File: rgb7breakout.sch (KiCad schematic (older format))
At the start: 2 parts

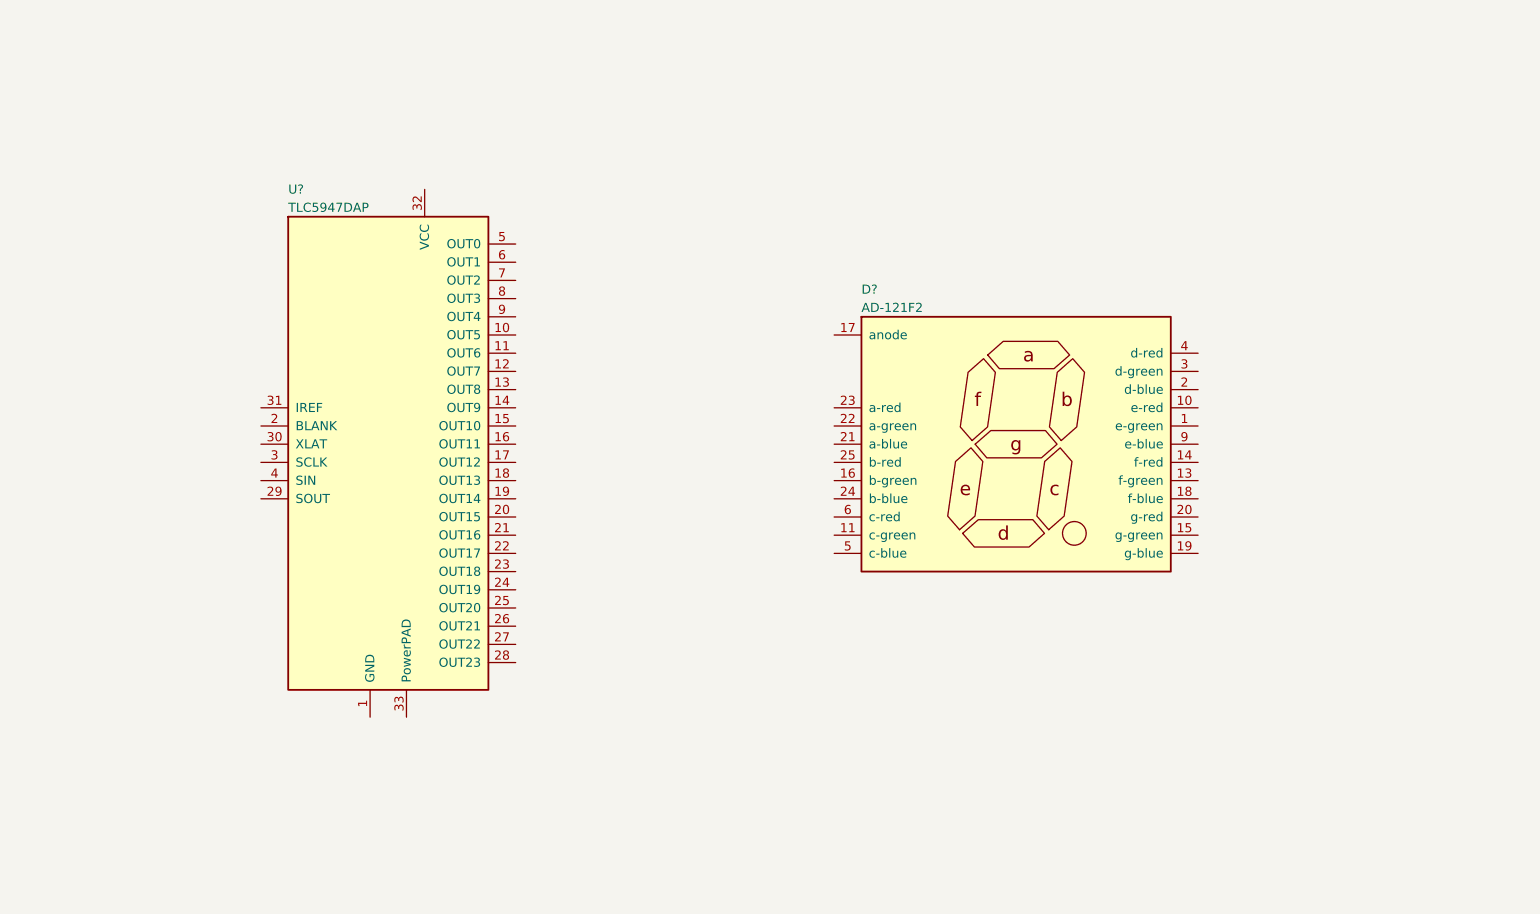
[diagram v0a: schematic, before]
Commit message: add RGB LED
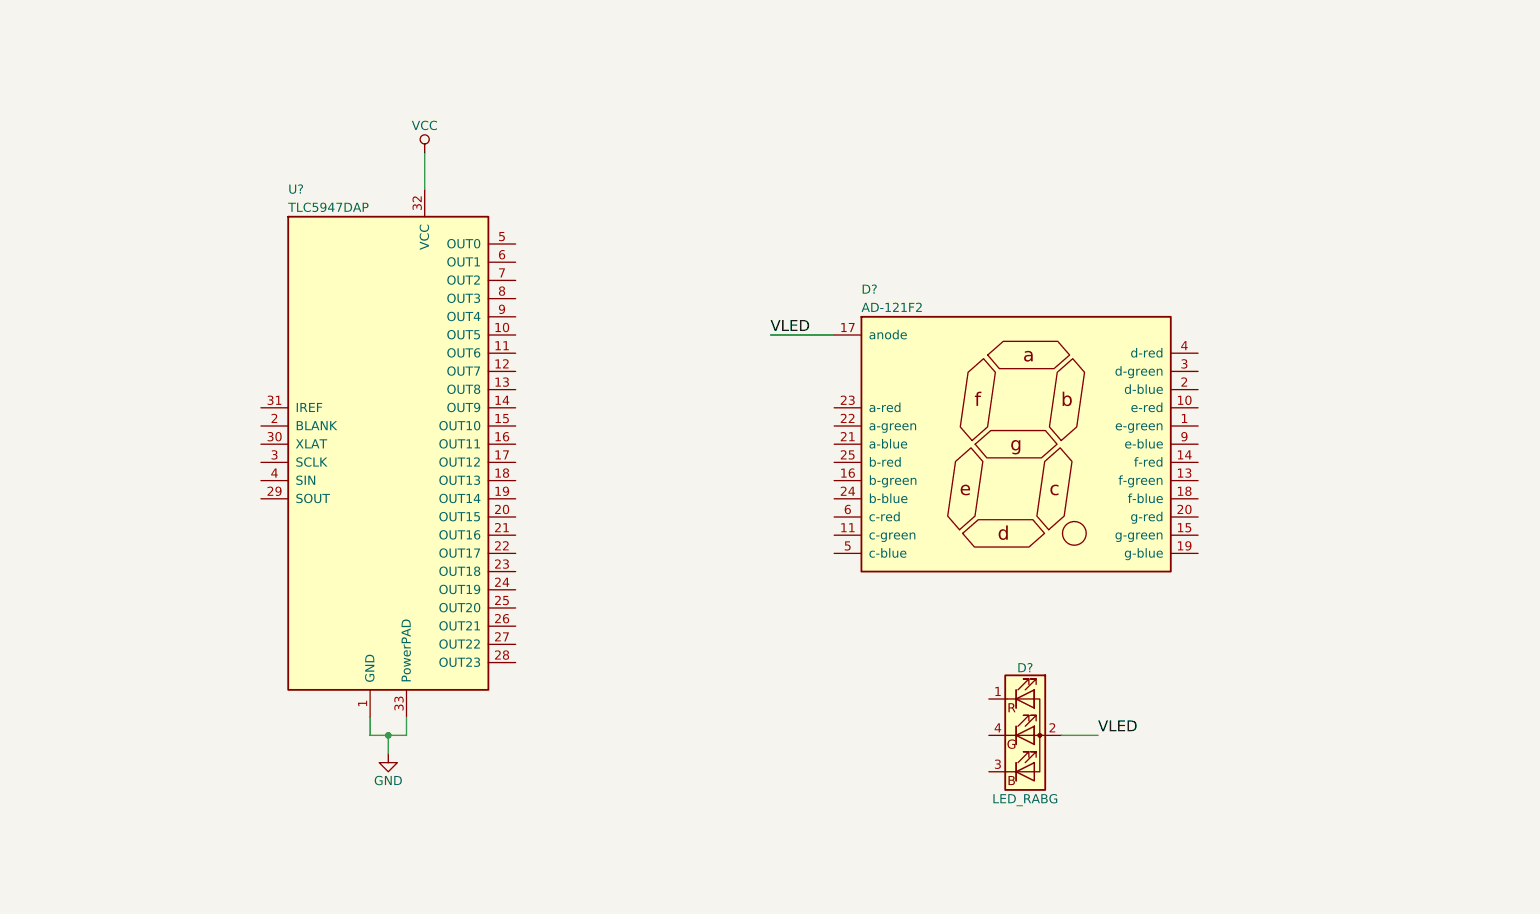
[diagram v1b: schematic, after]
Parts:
- added D?: LED_RABG, symbol LED_RABG
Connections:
- net VLED: now reaches D?.17 (anode)
- net VLED: now also D?.2 (A)
- net GND: now reaches U?.1 (GND)
- net GND: now also U?.33 (PowerPAD)
- net VCC: now reaches U?.32 (VCC)
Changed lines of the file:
@@
 	1    0    0    -1
 $EndComp
+$Comp
+L LED_RABG D?
+U 1 1 59B77822
+P 7000 5500
+F 0 "D?" H 7000 5870 50  0000 C CNN
+F 1 "LED_RABG" H 7000 5150 50  0000 C CNN
+F 2 "" H 7000 5450 50  0001 C CNN
+F 3 "" H 7000 5450 50  0001 C CNN
+	1    7000 5500
+	1    0    0    -1
+$EndComp
+$Comp
+L VCC #PWR?
+U 1 1 59B778E2
+P 3700 2300
+F 0 "#PWR?" H 3700 2150 50  0001 C CNN
+F 1 "VCC" H 3700 2450 50  0000 C CNN
+F 2 "" H 3700 2300 50  0001 C CNN
+F 3 "" H 3700 2300 50  0001 C CNN
+	1    3700 2300
+	1    0    0    -1
+$EndComp
+$Comp
+L GND #PWR?
+U 1 1 59B77905
+P 3500 5600
+F 0 "#PWR?" H 3500 5350 50  0001 C CNN
+F 1 "GND" H 3500 5450 50  0000 C CNN
+F 2 "" H 3500 5600 50  0001 C CNN
+F 3 "" H 3500 5600 50  0001 C CNN
+	1    3500 5600
+	1    0    0    -1
+$EndComp
+Wire Wire Line
+	3700 2300 3700 2500
+Wire Wire Line
+	3400 5400 3400 5500
+Wire Wire Line
+	3400 5500 3600 5500
+Wire Wire Line
+	3600 5500 3600 5400
+Wire Wire Line
+	3500 5600 3500 5500
+Connection ~ 3500 5500
+Text Label 5600 3300 0    60   ~ 0
+VLED
+Text Label 7400 5500 0    60   ~ 0
+VLED
+Wire Wire Line
+	5600 3300 5950 3300
+Wire Wire Line
+	7200 5500 7400 5500
 $EndSCHEMATC

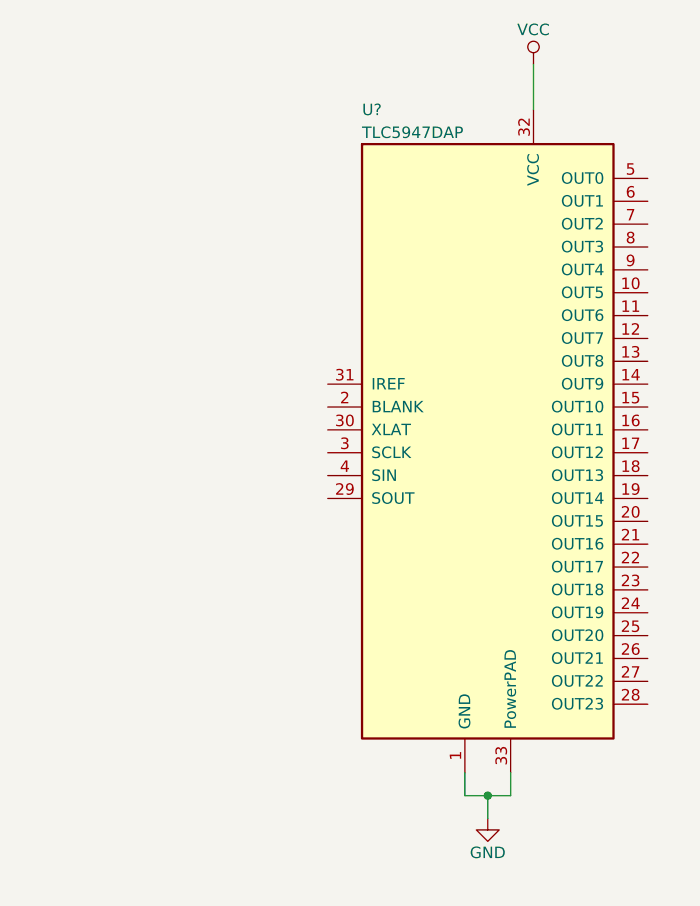
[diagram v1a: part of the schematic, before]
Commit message: add resistor and some wires
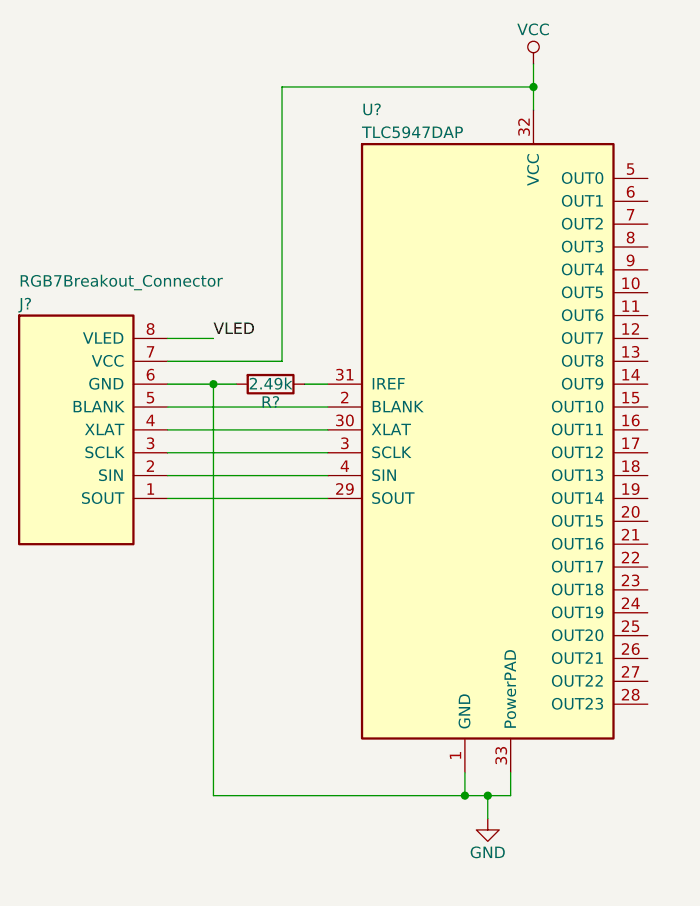
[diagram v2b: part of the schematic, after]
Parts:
- added J?: RGB7Breakout_Connector, symbol RGB7Breakout_Connector
- added R?: 2.49k, symbol R
- D?: Description (none) -> LED RGB DIFFUSED 4LCC SMD; ManufacturerPartNumber (none) -> CLV1A-FKB-CHMKPEHBB7A363
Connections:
- net GND: now also J?.6 (GND), R?.2
- net VCC: now also J?.7 (VCC)
- net VLED: now also J?.8 (VLED)
- net at U?.2 (BLANK): now also J?.5 (BLANK)
- net at U?.29 (SOUT): now also J?.1 (SOUT)
- net at U?.3 (SCLK): now also J?.3 (SCLK)
- net at U?.30 (XLAT): now also J?.4 (XLAT)
- net at U?.31 (IREF): now also R?.1
- net at U?.4 (SIN): now also J?.2 (SIN)
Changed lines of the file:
@@
 F 2 "" H 7000 5450 50  0001 C CNN
 F 3 "" H 7000 5450 50  0001 C CNN
+F 4 "CLV1A-FKB-CHMKPEHBB7A363" H 7000 5500 60  0001 C CNN "ManufacturerPartNumber"
+F 5 "LED RGB DIFFUSED 4LCC SMD" H 7000 5500 60  0001 C CNN "Description"
 	1    7000 5500
 	1    0    0    -1
@@
 	3400 5400 3400 5500
 Wire Wire Line
-	3400 5500 3600 5500
+	2300 5500 3600 5500
 Wire Wire Line
 	3600 5500 3600 5400
@@
 Wire Wire Line
 	7200 5500 7400 5500
+$Comp
+L RGB7Breakout_Connector J?
+U 1 1 59B77FB5
+P 1700 3900
+F 0 "J?" H 1450 4450 50  0000 L CNN
+F 1 "RGB7Breakout_Connector" H 1450 4550 50  0000 L CNN
+F 2 "" H 1700 3900 60  0001 C CNN
+F 3 "" H 1700 3900 60  0001 C CNN
+	1    1700 3900
+	1    0    0    -1
+$EndComp
+Wire Wire Line
+	2100 4200 2800 4200
+Wire Wire Line
+	2100 4100 2800 4100
+Wire Wire Line
+	2100 4000 2800 4000
+Wire Wire Line
+	2100 3900 2800 3900
+Wire Wire Line
+	2100 3800 2800 3800
+Text Label 2300 3500 0    50   ~ 0
+VLED
+Wire Wire Line
+	2100 3500 2300 3500
+Wire Wire Line
+	2100 3600 2600 3600
+Wire Wire Line
+	2600 3600 2600 2400
+Wire Wire Line
+	2600 2400 3700 2400
+Connection ~ 3700 2400
+Wire Wire Line
+	2100 3700 2400 3700
+Wire Wire Line
+	2300 3700 2300 5500
+Connection ~ 3400 5500
+$Comp
+L R R?
+U 1 1 59B782F7
+P 2550 3700
+F 0 "R?" V 2630 3700 50  0000 C CNN
+F 1 "2.49k" V 2550 3700 50  0000 C CNN
+F 2 "" V 2480 3700 50  0001 C CNN
+F 3 "" H 2550 3700 50  0001 C CNN
+F 4 "RC0603FR-072K49L" H 2550 3700 60  0001 C CNN "ManufacturerPartNumber"
+F 5 "RES SMD 2.49K OHM 1% 1/10W 0603" H 2550 3700 60  0001 C CNN "Description"
+	1    2550 3700
+	0    1    1    0
+$EndComp
+Wire Wire Line
+	2700 3700 2800 3700
+Connection ~ 2300 3700
 $EndSCHEMATC

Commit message: draw some more wires
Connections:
- net at D?.1 (e-green): now also U?.18 (OUT13)
- net at D?.10 (e-red): now also U?.17 (OUT12)
- net at D?.11 (c-green): now also U?.12 (OUT7)
- net at D?.13 (f-green): now also U?.21 (OUT16)
- net at D?.14 (f-red): now also U?.20 (OUT15)
- net at D?.16 (b-green): now also U?.9 (OUT4)
- net at D?.2 (d-blue): now also U?.16 (OUT11)
- net at D?.21 (a-blue): now also U?.7 (OUT2)
- net at D?.22 (a-green): now also U?.6 (OUT1)
- net at D?.23 (a-red): now also U?.5 (OUT0)
- net at D?.24 (b-blue): now also U?.10 (OUT5)
- net at D?.25 (b-red): now also U?.8 (OUT3)
- net at D?.3 (d-green): now also U?.15 (OUT10)
- net at D?.4 (d-red): now also U?.14 (OUT9)
- net at D?.5 (c-blue): now also U?.13 (OUT8)
- net at D?.6 (c-red): now also U?.11 (OUT6)
- net at D?.9 (e-blue): now also U?.19 (OUT14)
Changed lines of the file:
@@
 	2700 3700 2800 3700
 Connection ~ 2300 3700
+Wire Wire Line
+	4200 2800 5500 2800
+Wire Wire Line
+	5500 2800 5500 3700
+Wire Wire Line
+	5500 3700 5950 3700
+Wire Wire Line
+	4200 2900 5400 2900
+Wire Wire Line
+	5400 2900 5400 3800
+Wire Wire Line
+	5400 3800 5950 3800
+Wire Wire Line
+	4200 3000 5300 3000
+Wire Wire Line
+	5300 3000 5300 3900
+Wire Wire Line
+	5300 3900 5950 3900
+Wire Wire Line
+	4200 3100 5200 3100
+Wire Wire Line
+	5200 3100 5200 4000
+Wire Wire Line
+	5200 4000 5950 4000
+Wire Wire Line
+	4200 3200 5100 3200
+Wire Wire Line
+	5100 3200 5100 4100
+Wire Wire Line
+	5100 4100 5950 4100
+Wire Wire Line
+	4200 3300 5000 3300
+Wire Wire Line
+	5000 3300 5000 4200
+Wire Wire Line
+	5000 4200 5950 4200
+Wire Wire Line
+	4200 3400 4900 3400
+Wire Wire Line
+	4900 3400 4900 4300
+Wire Wire Line
+	4900 4300 5950 4300
+Wire Wire Line
+	4200 3500 4800 3500
+Wire Wire Line
+	4800 3500 4800 4400
+Wire Wire Line
+	4800 4400 5950 4400
+Wire Wire Line
+	4200 3600 4700 3600
+Wire Wire Line
+	4700 3600 4700 4500
+Wire Wire Line
+	4700 4500 5950 4500
+Wire Wire Line
+	4200 3700 4600 3700
+Wire Wire Line
+	4600 3700 4600 2700
+Wire Wire Line
+	4600 2700 8100 2700
+Wire Wire Line
+	8100 2700 8100 3400
+Wire Wire Line
+	8100 3400 7950 3400
+Wire Wire Line
+	4200 3800 4500 3800
+Wire Wire Line
+	4500 3800 4500 2600
+Wire Wire Line
+	4500 2600 8200 2600
+Wire Wire Line
+	8200 2600 8200 3500
+Wire Wire Line
+	8200 3500 7950 3500
+Wire Wire Line
+	4200 3900 4400 3900
+Wire Wire Line
+	4400 3900 4400 2500
+Wire Wire Line
+	4400 2500 8300 2500
+Wire Wire Line
+	8300 2500 8300 3600
+Wire Wire Line
+	8300 3600 7950 3600
+Wire Wire Line
+	4200 4000 4300 4000
+Wire Wire Line
+	4300 4000 4300 2400
+Wire Wire Line
+	4300 2400 8400 2400
+Wire Wire Line
+	8400 2400 8400 3700
+Wire Wire Line
+	8400 3700 7950 3700
+Wire Wire Line
+	4200 4100 4600 4100
+Wire Wire Line
+	4600 4100 4600 4700
+Wire Wire Line
+	4600 4700 8100 4700
+Wire Wire Line
+	8100 4700 8100 3800
+Wire Wire Line
+	8100 3800 7950 3800
+Wire Wire Line
+	4200 4200 4500 4200
+Wire Wire Line
+	4500 4200 4500 4800
+Wire Wire Line
+	4500 4800 8200 4800
+Wire Wire Line
+	8200 4800 8200 3900
+Wire Wire Line
+	8200 3900 7950 3900
+Wire Wire Line
+	4200 4300 4400 4300
+Wire Wire Line
+	4400 4300 4400 4900
+Wire Wire Line
+	4400 4900 8300 4900
+Wire Wire Line
+	8300 4900 8300 4000
+Wire Wire Line
+	8300 4000 7950 4000
+Wire Wire Line
+	4200 4400 4300 4400
+Wire Wire Line
+	4300 4400 4300 5000
+Wire Wire Line
+	4300 5000 8400 5000
+Wire Wire Line
+	8400 5000 8400 4100
+Wire Wire Line
+	8400 4100 7950 4100
 $EndSCHEMATC
